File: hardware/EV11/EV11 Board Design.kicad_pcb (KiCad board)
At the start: 4 copper layers, 66.4 x 89.3 mm, 103 parts, among them J1 Conn_01x02_Socket, J10 Conn_01x08_Socket, J11 Conn_01x06_Female, J2 Conn_01x06_Female, J3 Conn_01x06_Female, J4 AudioPlug4, J5 Conn_01x02_Socket, J9 USB_C_Receptacle, SW4 SW_Push, SW5 SW_Push, U1 STM32F405RGTx, U11 ESP32-S3-WROOM-1-N8R2, U13 BM14B(0.8)-24DS-0.4V(53), U2 BQ21040DBVR, U3 CH340C, U4 USBLC6-2P6, U5 STM32F030C8Tx, U6 WM8960CGEFL/RV, U7 TPS63060, Y1 Crystal_GND24

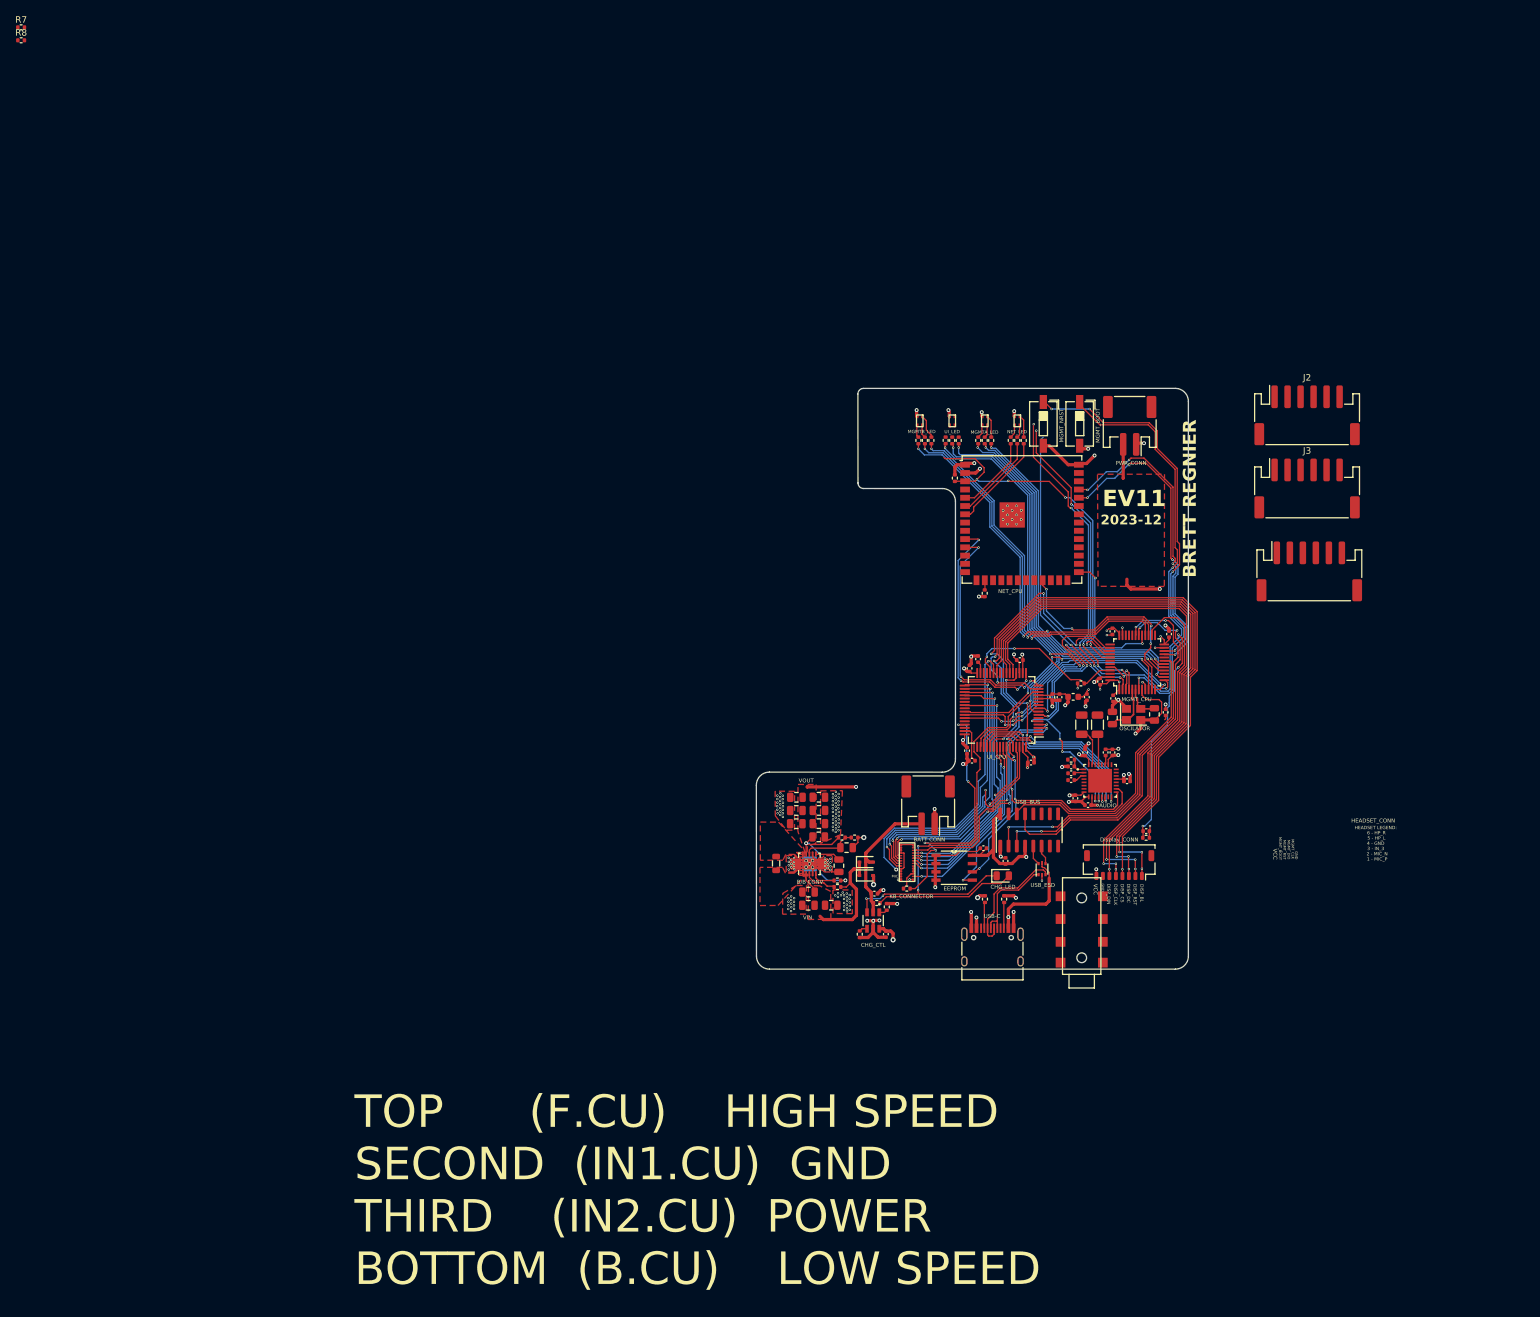
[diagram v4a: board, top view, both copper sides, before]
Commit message: Redesigning the power layout layers of EV11
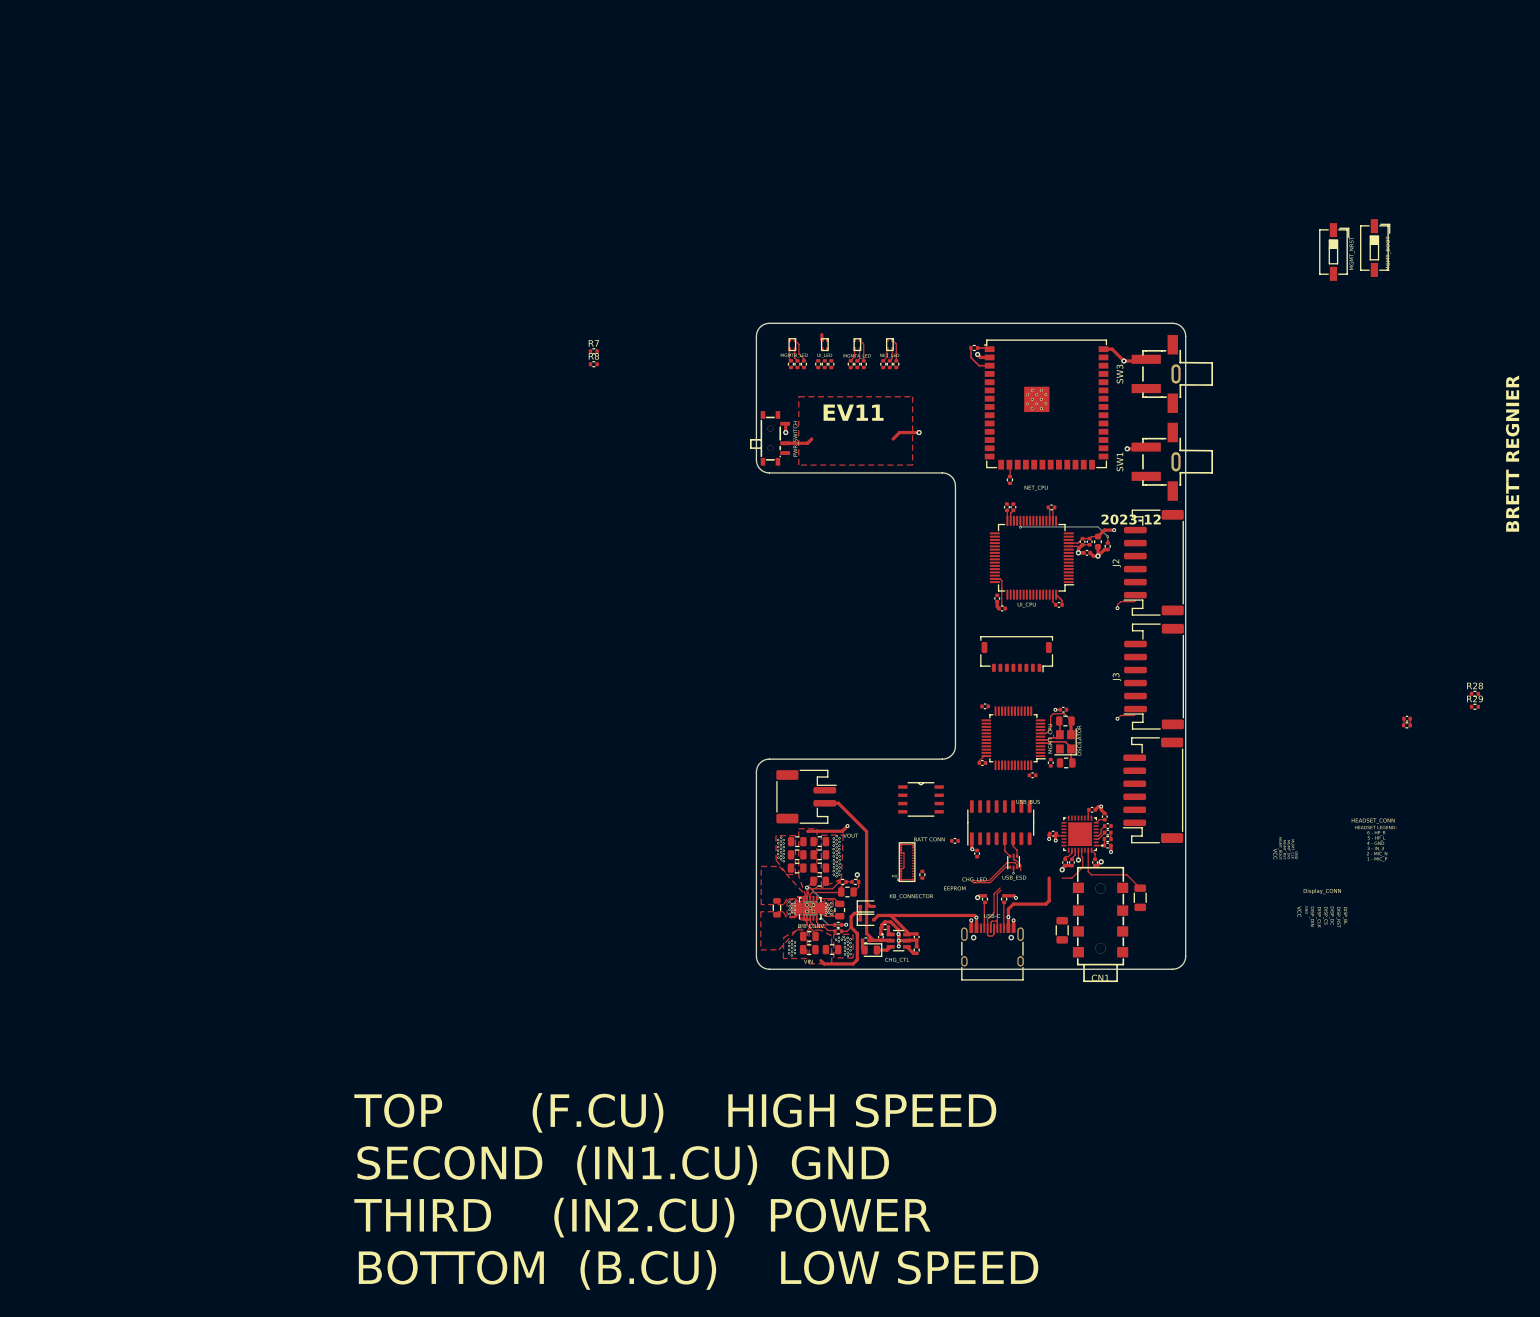
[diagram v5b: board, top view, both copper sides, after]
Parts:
- removed C17: 1u, Capacitor_SMD:C_0402_1005Metric
- removed J4: AudioPlug4, PJ_313E_8A:PJ_313E_8A
- removed J5: Conn_01x02_Socket, Connector_JST:JST_PH_S2B-PH-SM4-TB_1x02-1MP_P2.00mm_Horizontal
- added C5: 1u, Capacitor_SMD:C_0402_1005Metric, F.Cu at (168.0, 123.3)
- added CN1: PJ-313E-8A_C707222, PJ-313E-8A:AUDIO-SMD_PJ-313E-8A-EH, F.Cu at (166.9, 137.7)
- added R28: 0, Resistor_SMD:R_0402_1005Metric, F.Cu at (224.5, 103.0)
- added R29: 0, Resistor_SMD:R_0402_1005Metric, F.Cu at (224.5, 105.0)
- added SW1: TS-1037-A11B3-D2, TS-1037-A11B3-D2:KEY-SMD_2P-L7.1-W10.6-P4.00-LS9.0, F.Cu at (176.2, 67.3)
- added SW2: MSK12C02-HB, MSK12C02-HB:SW-TH_MSK12C02-HB-1, F.Cu at (116.7, 63.7)
- added SW3: TS-1037-A11B3-D2, TS-1037-A11B3-D2:KEY-SMD_2P-L7.1-W10.6-P4.00-LS9.0, F.Cu at (176.2, 53.8)
- moved R7 101.2 mm to (89.0, 50.3)
- moved R8 101.2 mm to (89.0, 52.3)
- moved SW4 52.8 mm to (209.0, 34.4)
- moved SW5 51.8 mm to (202.7, 35.0)
- moved R10 43.7 mm to (214.0, 107.8)
- moved C36 43.7 mm to (214.0, 106.8)
- moved J11 41.3 mm to (175.0, 117.8), turned to 90 degrees
- moved J3 37.3 mm to (175.1, 100.3), turned to 90 degrees
- moved J10 35.7 mm to (154.0, 97.3)
- moved J2 32.7 mm to (175.1, 82.8), turned to 90 degrees
- moved C29 32.1 mm to (161.0, 139.3), turned to -90 degrees
- moved C25 30.4 mm to (149.2, 104.9), turned to 180 degrees
- moved C34 28.4 mm to (148.7, 113.6), turned to 0 degrees
- moved C30 28.1 mm to (173.0, 134.3), turned to -90 degrees
- moved C14 25.4 mm to (152.5, 74.3)
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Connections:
- J10 pad 5: /DISP_SPI_SCK -> /SPI1_CLK
- J10 pad 6: /DISP_SPI_MOSI -> /SPI1_MOSI
- J2 pad 2: /MGMT_BOOT -> unconnected-(J2-Pin_2-Pad2)
- J2 pad 3: /MGMT_NRST -> unconnected-(J2-Pin_3-Pad3)
- J2 pad 4: /MGMT_SWDIO -> unconnected-(J2-Pin_4-Pad4)
- J2 pad 5: /MGMT_SWCLK -> unconnected-(J2-Pin_5-Pad5)
- J3 pad 2: /MGMT_BOOT -> unconnected-(J3-Pin_2-Pad2)
- J3 pad 3: /MGMT_NRST -> unconnected-(J3-Pin_3-Pad3)
- J3 pad 4: /MGMT_SWDIO -> unconnected-(J3-Pin_4-Pad4)
- J3 pad 5: /MGMT_SWCLK -> unconnected-(J3-Pin_5-Pad5)
- U1 pad 15: /DISP_CS -> unconnected-(U1-PA1-Pad15)
- U1 pad 20: /I2S_DACLRC -> unconnected-(U1-PA4-Pad20)
- U1 pad 21: /DISP_SPI_SCK -> unconnected-(U1-PA5-Pad21)
- U1 pad 23: /DISP_SPI_MOSI -> unconnected-(U1-PA7-Pad23)
- U1 pad 24: unconnected-(U1-PC4-Pad24) -> /DISP_BL
- U1 pad 25: unconnected-(U1-PC5-Pad25) -> /DISP_CS
- U1 pad 46: unconnected-(U1-PA13-Pad46) -> Net-(U1-PA13)
- U1 pad 49: unconnected-(U1-PA14-Pad49) -> Net-(U1-PA14)
- U1 pad 50: /DISP_BL -> /I2S_DACLRC
- U1 pad 55: /KB_ROW6 -> /SPI1_CLK
- U1 pad 56: /KB_ROW7 -> /SPI1_MISO
- U1 pad 57: /KB_COL5 -> /SPI1_MOSI
- U6 pad 4: unconnected-(U6-LINPUT1-Pad4) -> Net-(U6-LINPUT1)
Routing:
- net Net-(J5-Pin_1): track 166.6 -> 0.00 mm, vias 2 -> 0
- net GND: track 498.3 -> 369.0 mm, vias 149 -> 131
- net Net-(U7-VOUT): track 19.4 -> 129.0 mm, vias 2 -> 4
- net /DISP_BL: track 104.2 -> 0.00 mm, vias 5 -> 0
- net /MGMT_BOOT: track 102.7 -> 1.04 mm, vias 5 -> 0
- net /DISP_CS: track 94.1 -> 0.00 mm, vias 3 -> 0
- net /DISP_RSTR: track 85.8 -> 0.00 mm, vias 3 -> 0
- net /DISP_DC: track 85.1 -> 0.00 mm, vias 3 -> 0
- net /DISP_SPI_MOSI: track 82.3 -> 0.00 mm, vias 1 -> 0
- net /DISP_SPI_SCK: track 82.3 -> 0.00 mm, vias 3 -> 0
- net +3.3V: track 329.3 -> 251.8 mm, vias 22 -> 5
- net /MGMT_NRST: track 74.0 -> 0.00 mm, vias 4 -> 0
- net /BATTERY_MON: track 70.0 -> 2.32 mm, vias 4 -> 0
- net /LEDB_R: track 64.8 -> 0.00 mm, vias 4 -> 0
- net /USB_TX1_MGMT: track 61.5 -> 0.00 mm, vias 4 -> 0
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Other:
- board size 66.4 x 89.3 mm -> 66 x 99.3 mm
- board text added: "PWR_SWITCH"
- board text removed: "AUDIO"
- board text removed: "PWR_CONN"

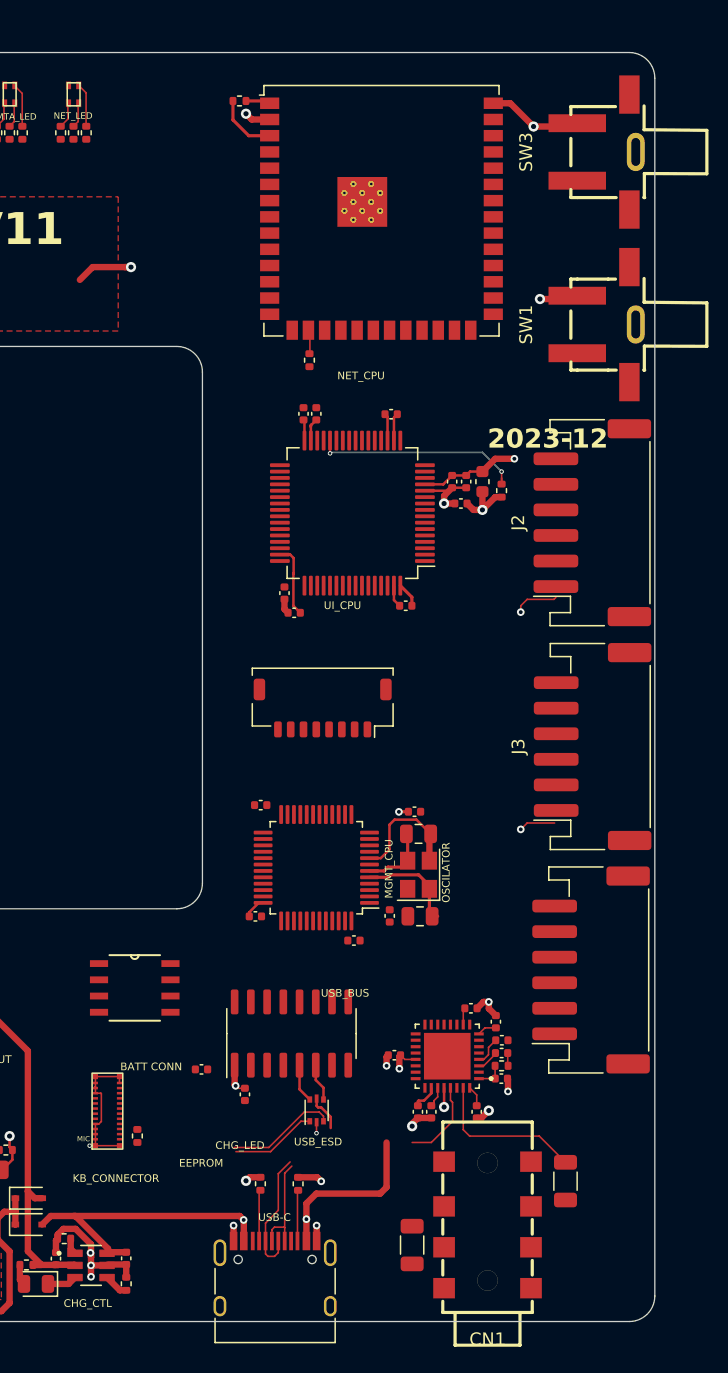
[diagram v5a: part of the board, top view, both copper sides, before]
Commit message: Added more changed pins and adding more traces to EV11
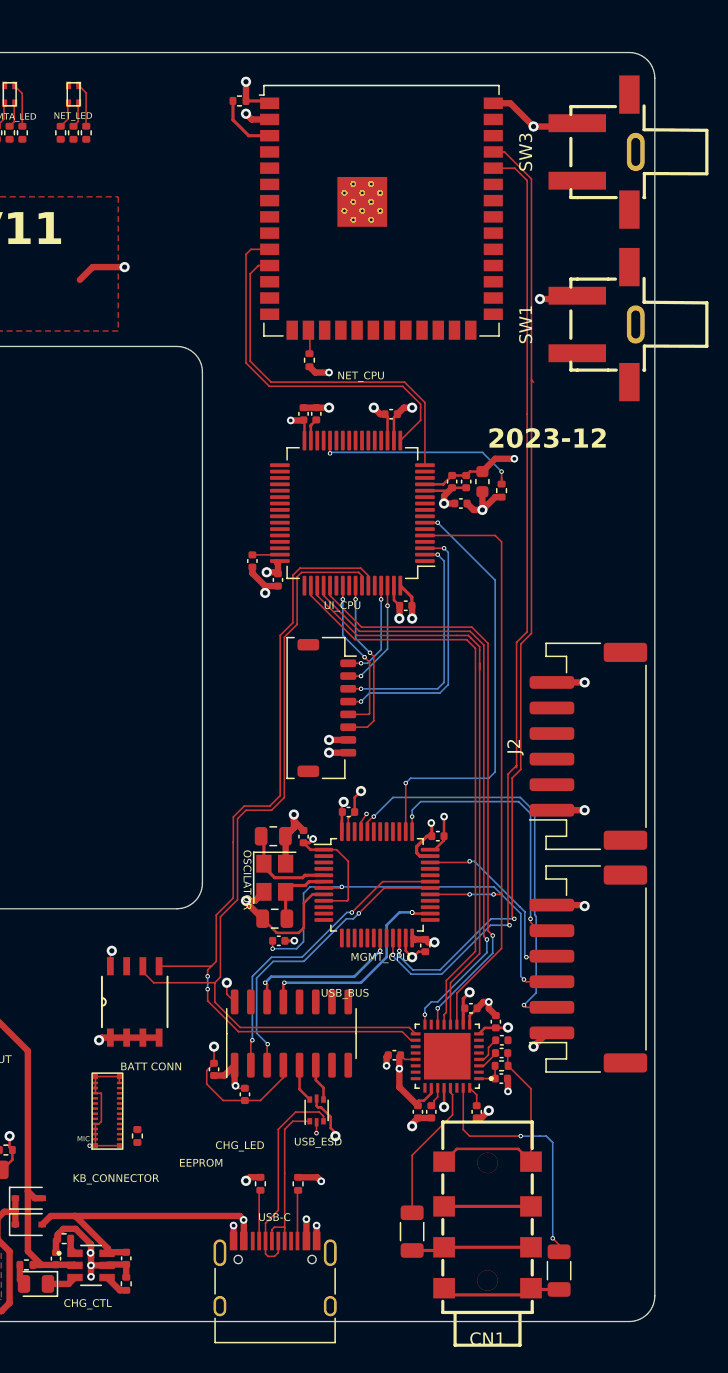
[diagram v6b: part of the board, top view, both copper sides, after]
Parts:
- removed J3: Conn_01x06_Female, Connector_JST:JST_PH_S6B-PH-SM4-TB_1x06-1MP_P2.00mm_Horizontal
- moved J2 17.5 mm to (174.8, 100.3)
- moved C25 16.9 mm to (162.0, 115.9), turned to -90 degrees
- moved C34 15.6 mm to (163.0, 107.3), turned to 180 degrees
- moved C35 14.7 mm to (150.6, 115.5), turned to 180 degrees
- moved C4 13.1 mm to (150.1, 107.3), turned to 180 degrees
- moved C23 13.1 mm to (150.3, 113.8), turned to 0 degrees
- moved Y1 11.3 mm to (150.3, 110.6), turned to -90 degrees
- moved C26 10.1 mm to (156.0, 105.4), turned to 0 degrees
- moved C24 9.16 mm to (152.5, 107.4), turned to 90 degrees
- moved C30 7.02 mm to (172.5, 141.3)
- moved C22 5.21 mm to (148.5, 85.8), turned to 90 degrees
- moved U5 4.93 mm to (158.3, 111.1), turned to 0 degrees
- moved C13 1.15 mm to (150.5, 87.3)
- moved CR1 1.10 mm to (139.3, 120.3), turned to 90 degrees
- moved C29 1.05 mm to (161.0, 138.3)
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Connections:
- U1 pad 2: unconnected-(U1-PC13-Pad2) -> /DISP_DC
- U1 pad 22: /DISP_RSTR -> unconnected-(U1-PA6-Pad22)
- U1 pad 24: /DISP_BL -> unconnected-(U1-PC4-Pad24)
- U1 pad 25: /DISP_CS -> unconnected-(U1-PC5-Pad25)
- U1 pad 26: /DISP_DC -> unconnected-(U1-PB0-Pad26)
- U1 pad 3: /KB_COL3 -> /DISP_CS
- U1 pad 61: /KB_COL2 -> /DISP_BL
- U1 pad 62: /KB_COL1 -> /DISP_RSTR
- U6 pad 2: Net-(U6-LINPUT3) -> unconnected-(U6-LINPUT3-Pad2)
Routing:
- net GND: track 369.0 -> 555.9 mm, vias 131 -> 146
- net +3.3V: track 251.8 -> 373.8 mm, vias 5 -> 19
- net /NET_TX1_MGMT: track 0.00 -> 75.2 mm, vias 0 -> 2
- net /NET_RX1_MGMT: track 0.00 -> 74.9 mm, vias 0 -> 2
- net /UI_SCL: track 0.00 -> 66.4 mm
- net /UI_SDA: track 0.00 -> 66.0 mm, vias 0 -> 2
- net /MCLK: track 0.00 -> 51.1 mm, vias 0 -> 2
- net /I2S_ADCDAT: track 0.00 -> 47.0 mm, vias 0 -> 2
- net /I2S_DACDAT: track 0.00 -> 46.5 mm, vias 0 -> 2
- net /I2S_BCLK: track 0.00 -> 46.2 mm
- net /I2S_DACLRC: track 0.00 -> 45.8 mm
- net /MGMT_NRST: track 0.00 -> 34.1 mm, vias 0 -> 3
- net /UI_RST: track 0.00 -> 33.5 mm, vias 0 -> 2
- net /MGMT_BOOT: track 1.04 -> 34.0 mm, vias 0 -> 2
- net /UI_RX2_NET: track 0.00 -> 29.0 mm
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
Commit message: Finished EV11 schematic and PCB
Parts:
- removed CR1: M24C02-RDW6TP, ESP32-S3-WROOM-1-N8R2:New_ESP32_M24C02-RMN6TP
- removed J11, J2: Conn_01x06_Female, Connector_JST:JST_PH_S6B-PH-SM4-TB_1x06-1MP_P2.00mm_Horizontal
- removed R41: 0, Resistor_SMD:R_0402_1005Metric
- removed U5: STM32F030C8Tx, Package_QFP:LQFP-48_7x7mm_P0.5mm
- added CN2: X1270WVS-2X05B-6TV01, X1270WVS-2x05B-6TV01:IDC-SMD_10P-P1.27_X1270WVS-2X05B-6TV01, F.Cu at (176.6, 84.8)
- added CN3: WAFER-SH1.0-6PWB, WAFER-SH1.0-6PWB:CONN-SMD_6P-P1.00_XUNPU_WAFER-SH1.0-6PWB, F.Cu at (176.6, 104.9)
- added CN4: WAFER-SH1.0-6PWB, WAFER-SH1.0-6PWB:CONN-SMD_6P-P1.00_XUNPU_WAFER-SH1.0-6PWB, F.Cu at (176.5, 96.0)
- added EEPROM: M24C02-RMN6TP, M24C02-RMN6TP:SOIC-8_L4.9-W3.9-P1.27-LS6.0-BL, F.Cu at (139.0, 130.3)
- added R30: 0, Resistor_SMD:R_0402_1005Metric, F.Cu at (139.0, 121.3)
- added U8: STM32F072C8T6, STM32F072C8T6:LQFP-48_L7.0-W7.0-P0.50-LS9.0-BL, F.Cu at (158.3, 111.1)
- moved C36 101.9 mm to (127.0, 53.8), turned to -90 degrees
- moved R10 101.6 mm to (128.0, 53.8), turned to -90 degrees
- moved SW4 86.7 mm to (124.0, 51.3), turned to 90 degrees
- moved SW5 85.3 mm to (119.0, 51.3), turned to 90 degrees
- moved R29 72.9 mm to (172.0, 54.3)
- moved R7 72.8 mm to (150.5, 89.3), turned to 90 degrees
- moved R8 72.6 mm to (151.5, 89.3), turned to 90 degrees
- moved R28 58.9 mm to (174.5, 71.8)
- moved R23 51.9 mm to (174.5, 61.8)
- moved R24 51.9 mm to (175.5, 61.8)
- moved D5 51.9 mm to (175.1, 58.1)
- moved R25 51.9 mm to (176.5, 61.8)
- moved R18 41.1 mm to (173.5, 61.8)
- moved D4 39.2 mm to (172.1, 58.1)
- moved R17 39.2 mm to (172.5, 61.8)
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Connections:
- C34 pad 1: +3.3V -> GND
- C34 pad 2: GND -> +3.3V
- C5 pad 1: /MIC_N -> GND
- CN1 pad 4: unconnected-(CN1-Pad4) -> GND
- R28 pad 1: Net-(U1-PA13) -> Net-(U1-PA0)
- R29 pad 1: Net-(U1-PA14) -> Net-(U1-PA1)
- U1 pad 14: /BATTERY_MON -> Net-(U1-PA0)
- U1 pad 15: unconnected-(U1-PA1-Pad15) -> Net-(U1-PA1)
- U1 pad 22: unconnected-(U1-PA6-Pad22) -> /BATTERY_MON
- U1 pad 23: unconnected-(U1-PA7-Pad23) -> /KB_ROW4
- U1 pad 24: unconnected-(U1-PC4-Pad24) -> /KB_ROW5
- U1 pad 25: unconnected-(U1-PC5-Pad25) -> /KB_ROW6
- U1 pad 26: unconnected-(U1-PB0-Pad26) -> Net-(U1-PB0)
- U1 pad 27: /KB_MIC -> /KB_ROW7
- U1 pad 34: /KB_ROW2 -> /KB_COL1
- U1 pad 35: /KB_ROW3 -> /KB_ROW2
- U1 pad 36: /KB_ROW4 -> /KB_COL2
- U1 pad 37: unconnected-(U1-PC6-Pad37) -> /KB_COL3
- U1 pad 38: unconnected-(U1-PC7-Pad38) -> /KB_COL4
- U1 pad 39: /KB_ROW5 -> /KB_ROW3
- U1 pad 4: /KB_COL4 -> /UI_LED_R
- U1 pad 40: unconnected-(U1-PC9-Pad40) -> /KB_COL5
- U1 pad 45: Net-(U1-PA12) -> unconnected-(U1-PA12-Pad45)
- U1 pad 46: Net-(U1-PA13) -> /UI_SWDIO
- U1 pad 49: Net-(U1-PA14) -> /UI_SWCLK
- U1 pad 54: /UI_LED_R -> unconnected-(U1-PD2-Pad54)
- U11 pad 29: unconnected-(U11-IO36-Pad29) -> /NET_LED_R
- U11 pad 30: unconnected-(U11-IO37-Pad30) -> /NET_LED_G
- U11 pad 31: unconnected-(U11-IO38-Pad31) -> /NET_LED_B
- U11 pad 32: unconnected-(U11-IO39-Pad32) -> /NET_MTCK
- U11 pad 33: unconnected-(U11-IO40-Pad33) -> /NET_MTDO
- U11 pad 34: unconnected-(U11-IO41-Pad34) -> /NET_MTDI
- U11 pad 35: unconnected-(U11-IO42-Pad35) -> /NET_MTMS
- U11 pad 5: /NET_LED_R -> unconnected-(U11-IO5-Pad5)
- U11 pad 6: /NET_LED_G -> unconnected-(U11-IO6-Pad6)
- U11 pad 7: /NET_LED_B -> unconnected-(U11-IO7-Pad7)
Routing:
- net /BATTERY_MON: track 2.32 -> 112.5 mm, vias 0 -> 2
- net /MGMT_NRST: track 34.1 -> 138.4 mm, vias 3 -> 5
- net /NET_RST: track 4.86 -> 90.5 mm, vias 0 -> 4
- net /MGMT_BOOT: track 34.0 -> 118.0 mm, vias 2 -> 4
- net GND: track 555.9 -> 631.3 mm, vias 146 -> 149
- net /KB_ROW4: track 0.00 -> 68.5 mm, vias 0 -> 2
- net /KB_ROW5: track 0.00 -> 68.1 mm, vias 0 -> 2
- net /KB_ROW6: track 0.00 -> 67.7 mm, vias 0 -> 2
- net /KB_ROW7: track 0.03 -> 67.3 mm, vias 0 -> 2
- net Net-(U1-PB0): track 0.00 -> 65.5 mm, vias 0 -> 2
- net /LEDA_B: track 0.00 -> 64.8 mm, vias 0 -> 2
- net /LEDA_G: track 0.00 -> 63.9 mm, vias 0 -> 2
- net /LEDA_R: track 0.00 -> 62.9 mm, vias 0 -> 2
- net /LEDB_G: track 0.00 -> 62.9 mm, vias 0 -> 2
- net /LEDB_B: track 0.00 -> 62.1 mm, vias 0 -> 2
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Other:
- board text added: "MAIN_CPU"
- board text removed: "EEPROM"
- board text removed: "UI_CPU"
